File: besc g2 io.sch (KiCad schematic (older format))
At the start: 30 parts

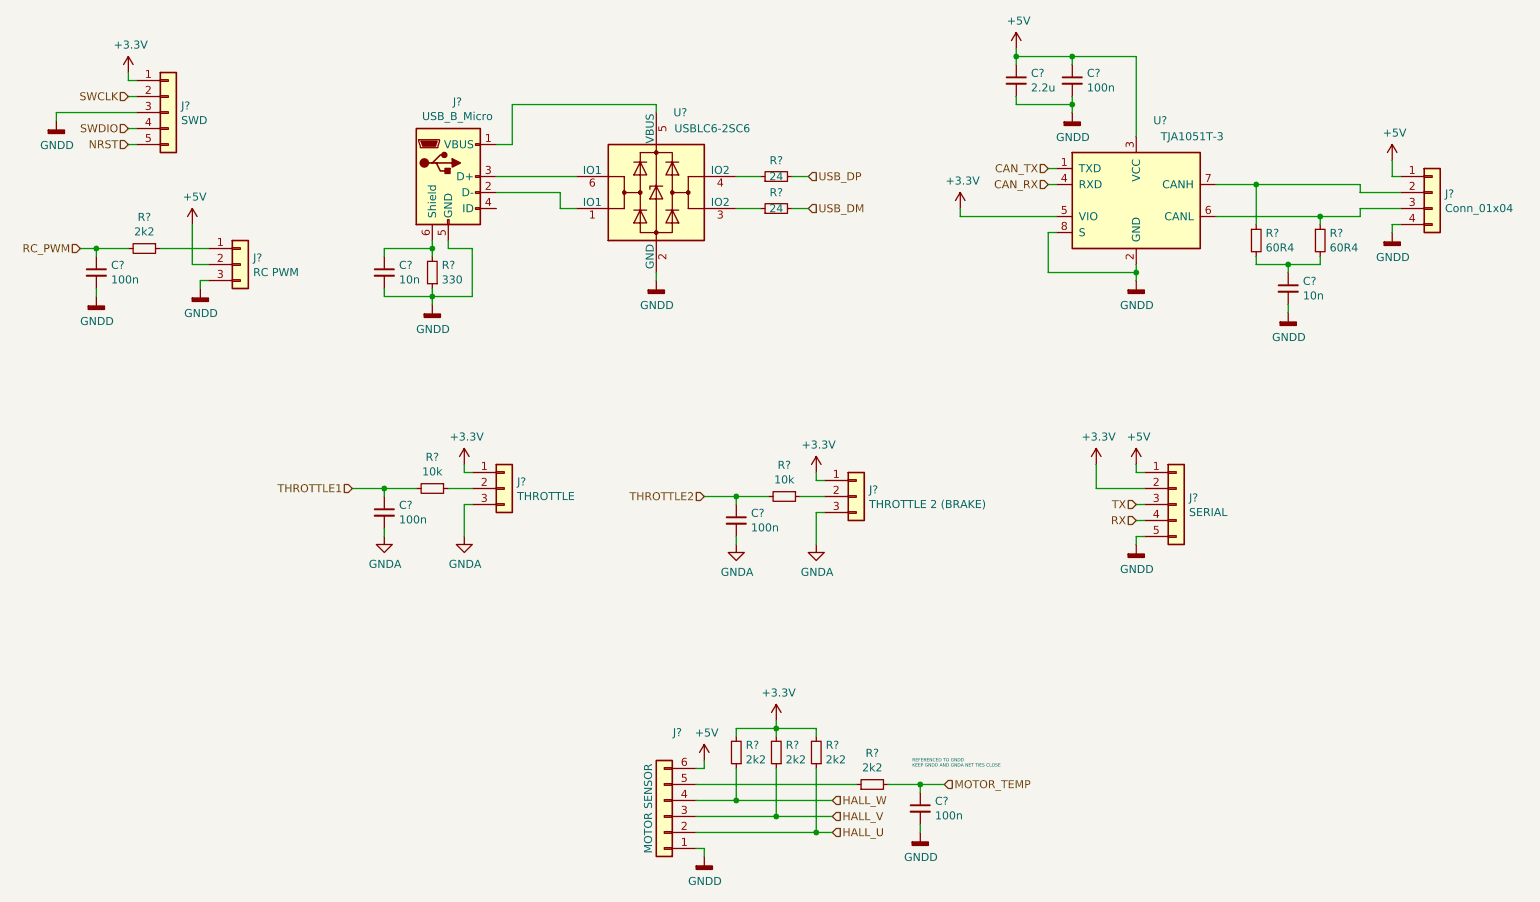
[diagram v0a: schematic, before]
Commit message: power stage layout draft
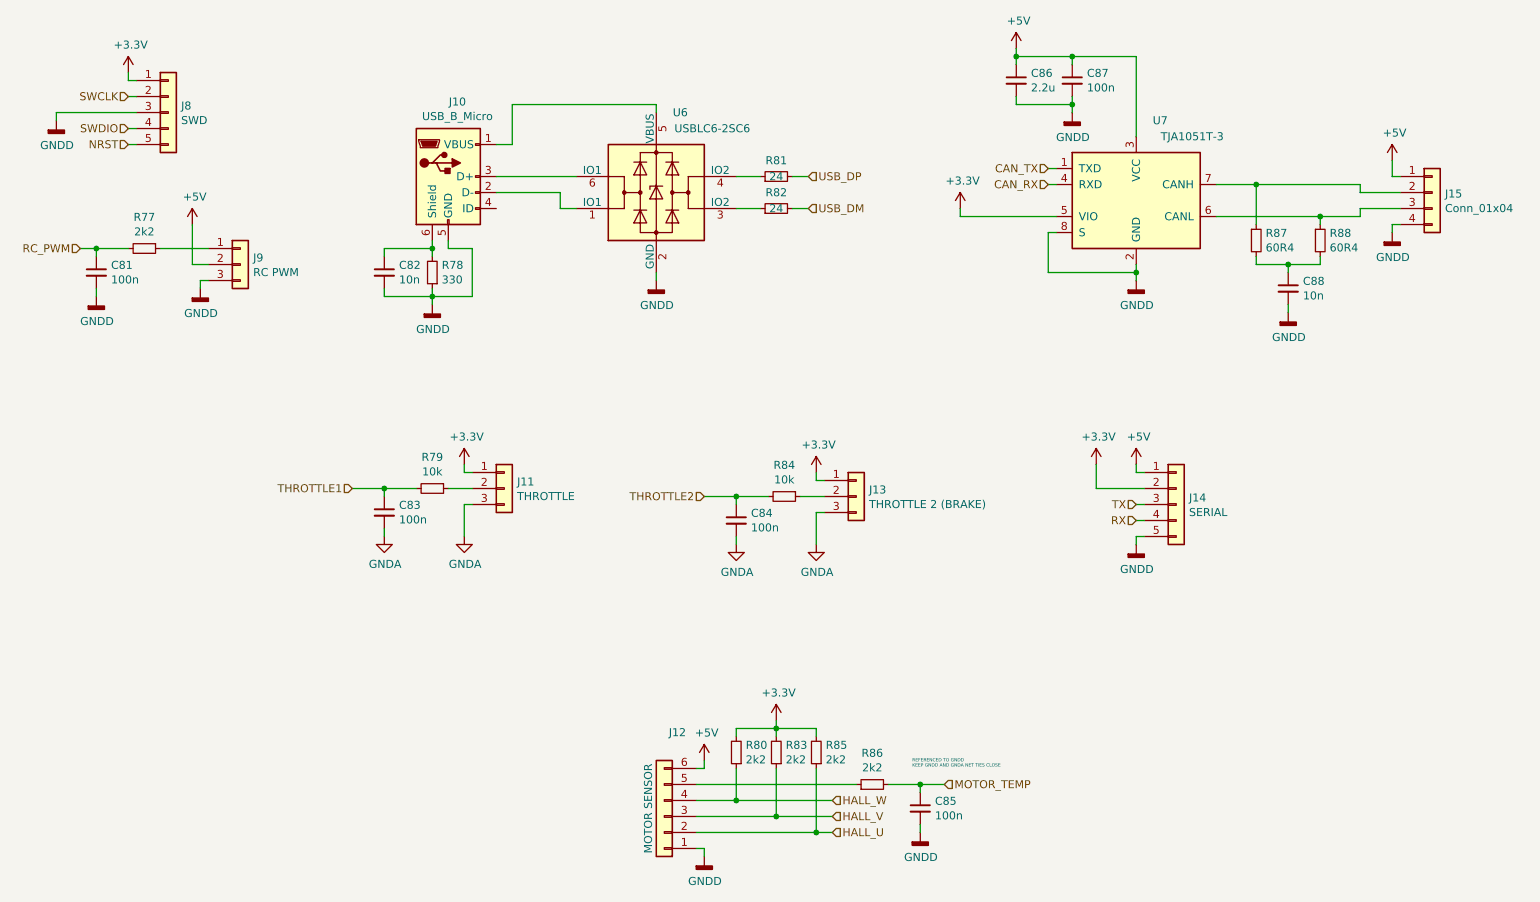
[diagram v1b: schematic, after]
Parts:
- C81, C82, C83, C84, C85, C86, C87, C88: renamed from C?; footprint (none) -> Capacitor_SMD:C_0603_1608Metric
- J10: renamed from J?; footprint (none) -> Connector_USB:USB_Micro-B_Molex_47346-0001
- J11: renamed from J?; footprint (none) -> Connector_PinHeader_2.54mm:PinHeader_1x03_P2.54mm_Vertical_SMD_Pin1Right
- J12: renamed from J?; footprint (none) -> Connector_PinHeader_2.54mm:PinHeader_1x06_P2.54mm_Vertical
- J13, J9: renamed from J?; footprint (none) -> Connector_PinHeader_2.54mm:PinHeader_1x03_P2.54mm_Vertical
- J14, J8: renamed from J?; footprint (none) -> Connector_PinHeader_2.54mm:PinHeader_1x05_P2.54mm_Vertical
- J15: renamed from J?; footprint (none) -> Connector_PinHeader_2.54mm:PinHeader_1x04_P2.54mm_Vertical
- R77, R78, R79, R80, R81, R82, R83, R84, R85, R86, R87, R88: renamed from R?; footprint (none) -> Resistor_SMD:R_0603_1608Metric
- gave numbers to parts that had none: 2

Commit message: isolated drivers, layout
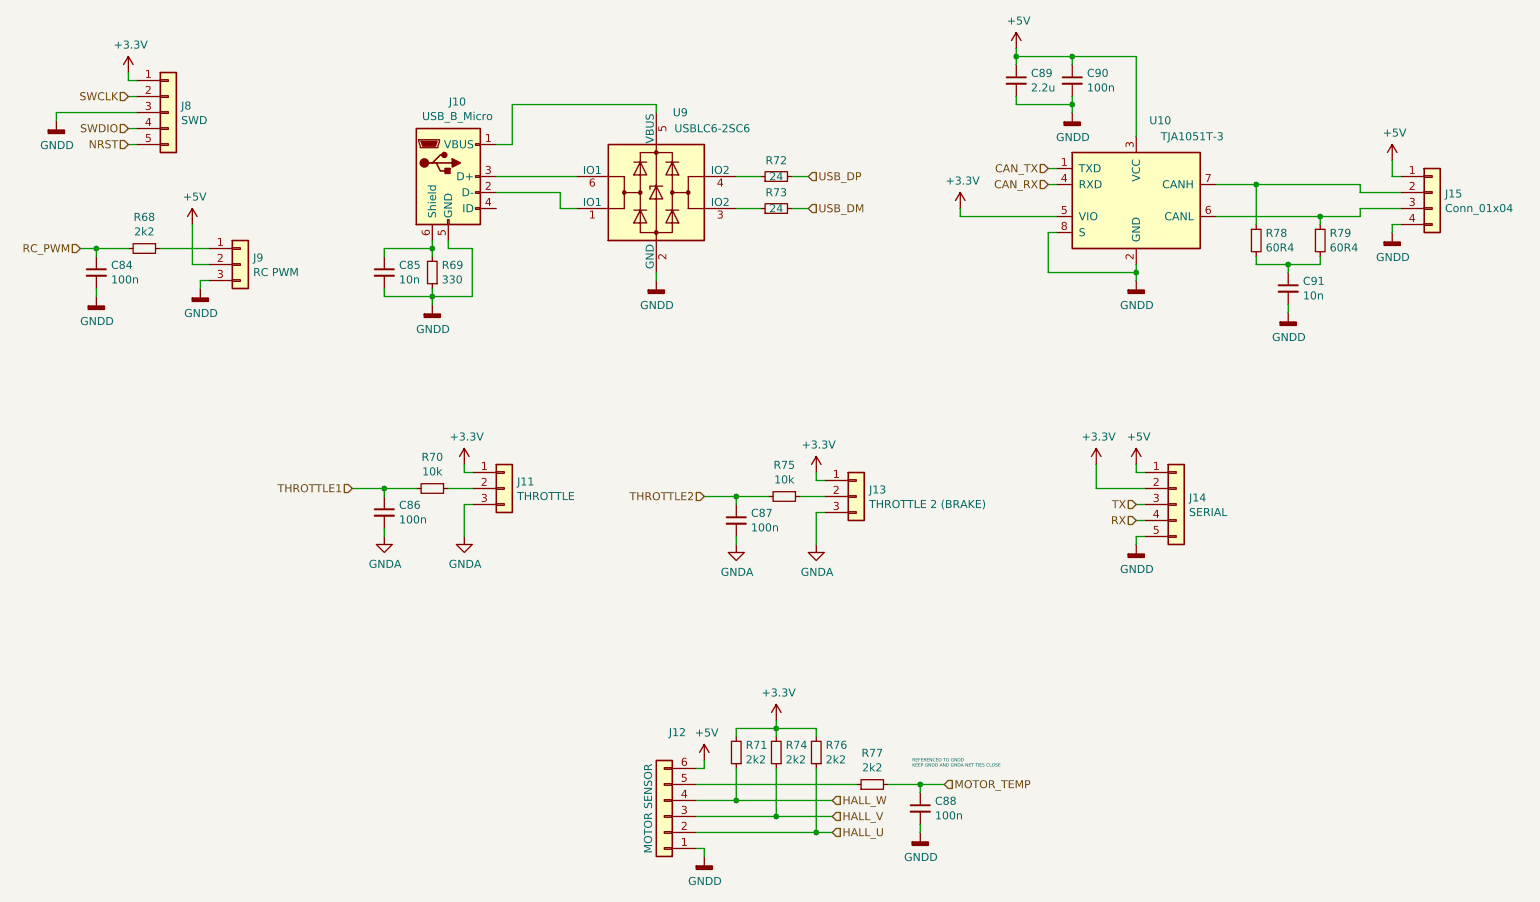
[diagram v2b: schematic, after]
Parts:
- renumbered C81 to C84, C82 to C85, C83 to C86, C84 to C87, C85 to C88, C86 to C89, C87 to C90, C88 to C91, R77 to R68, R78 to R69, R79 to R70, R80 to R71, R81 to R72, R82 to R73, R83 to R74, R84 to R75, R85 to R76, R86 to R77, R87 to R78, R88 to R79, U7 to U10, U6 to U9

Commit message: 12V PS, isolated gate drivers
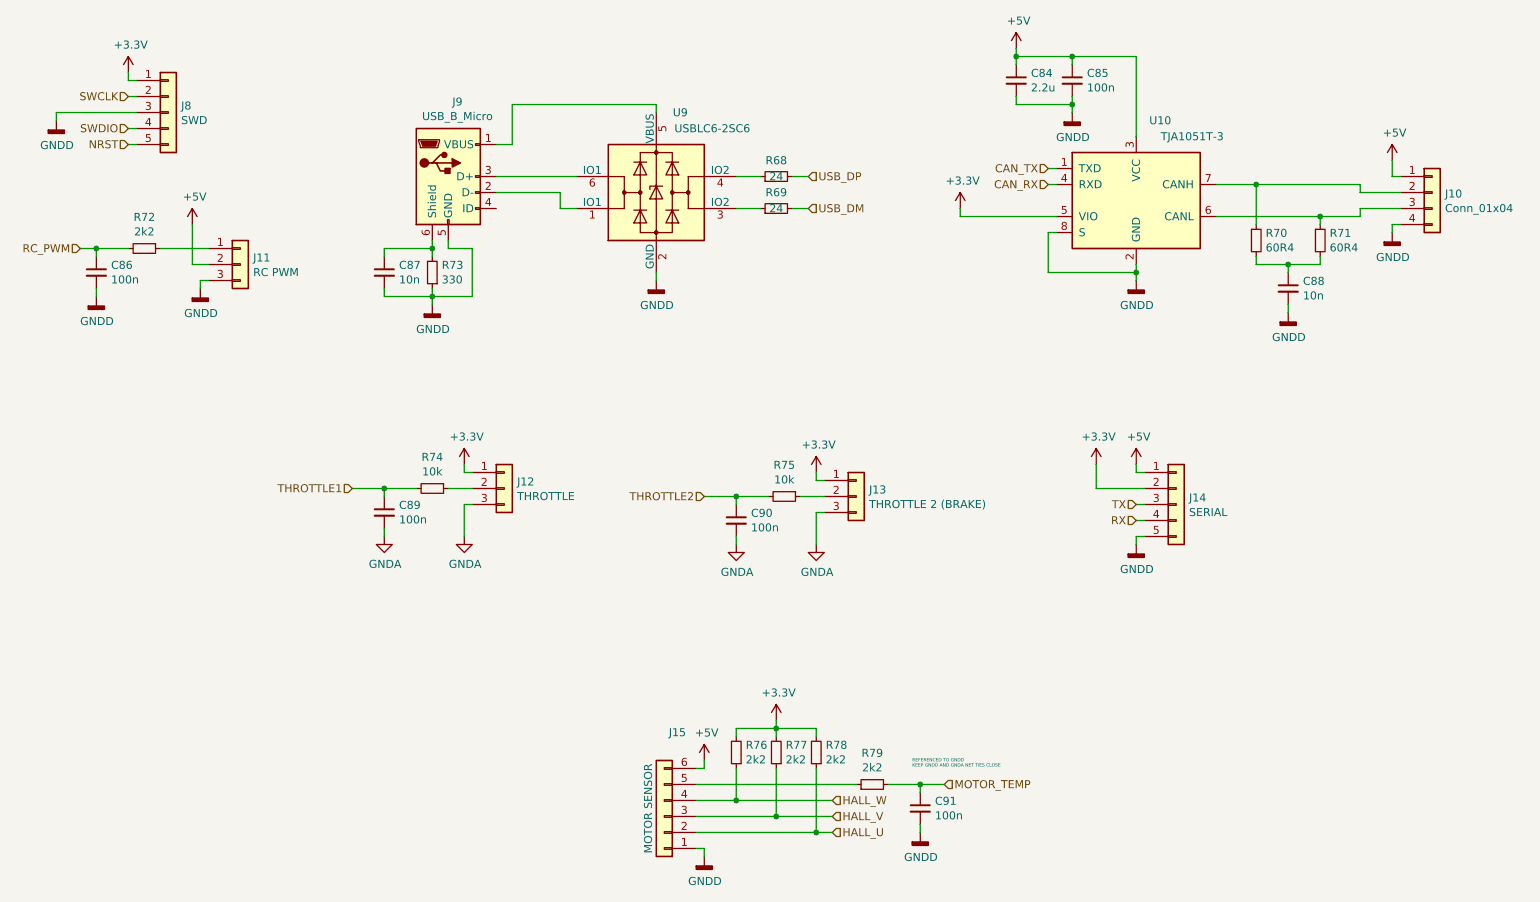
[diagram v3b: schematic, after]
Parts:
- renumbered C89 to C84, C90 to C85, C84 to C86, C85 to C87, C91 to C88, C86 to C89, C87 to C90, C88 to C91, J15 to J10, J9 to J11, J11 to J12, J12 to J15, J10 to J9, R72 to R68, R73 to R69, R78 to R70, R79 to R71, R68 to R72, R69 to R73, R70 to R74, R71 to R76, R74 to R77, R76 to R78, R77 to R79

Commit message: layout and routing progress
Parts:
- added D7: ESD 100V, Diode_SMD:D_SOD-123, symbol Device:D_Zener
- added J15: IGNITION, Connector_PinHeader_2.54mm:PinHeader_1x02_P2.54mm_Vertical, symbol Connector_Generic:Conn_01x02
- added R84, R85: 10k, Resistor_SMD:R_0603_1608Metric, symbol Device:R_Small
- J10: renamed from J9; footprint Connector_USB:USB_Micro-B_Molex_47346-0001 -> Connector_USB:USB_Micro-B_Wuerth_614105150721_Vertical_CircularHoles
- J11: renamed from J12; footprint Connector_PinHeader_2.54mm:PinHeader_1x03_P2.54mm_Vertical_SMD_Pin1Right -> Connector_PinHeader_2.54mm:PinHeader_1x03_P2.54mm_Vertical
- renumbered C86 to C84, C87 to C85, C89 to C86, C90 to C87, C91 to C88, C84 to C89, C85 to C90, C88 to C91, J15 to J12, J10 to J16, J11 to J9, R72 to R73, R73 to R74, R74 to R75, R68 to R77, R69 to R78, R77 to R79, R75 to R80, R78 to R81, R79 to R82, R70 to R83, R71 to R86
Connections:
- net GNDD: now also D7.2 (A)
- new net: J15.1 (Pin_1), R84.1
- new net: J15.2 (Pin_2), R85.1
- new net IGNITION: D7.1 (K), R85.2
- new net VDC: R84.2
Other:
- note added: "SHORT TO RUN"

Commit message: finished routing
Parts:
- J16: value Conn_01x04 -> CAN
- U9: footprint Package_TO_SOT_SMD:SOT-23-6 -> Package_TO_SOT_SMD:SOT-666
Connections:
- net at U9.1 (IO1): now also R77.1; no longer J10.2 (D-)
- net at U9.4 (IO2): now also J10.2 (D-); no longer R77.1
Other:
- moved on the sheet: R77
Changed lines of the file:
@@
 P 9800 1850
 F 0 "J16" H 9880 1842 50  0000 L CNN
-F 1 "Conn_01x04" H 9880 1751 50  0000 L CNN
+F 1 "CAN" H 9880 1751 50  0000 L CNN
 F 2 "Connector_PinHeader_2.54mm:PinHeader_1x04_P2.54mm_Vertical" H 9800 1850 50  0001 C CNN
 F 3 "~" H 9800 1850 50  0001 C CNN
@@
 F 0 "U9" H 5100 2350 50  0000 C CNN
 F 1 "USBLC6-2SC6" H 5300 2250 50  0000 C CNN
-F 2 "Package_TO_SOT_SMD:SOT-23-6" H 4200 2250 50  0001 C CNN
+F 2 "Package_TO_SOT_SMD:SOT-666" H 4200 2250 50  0001 C CNN
 F 3 "http://www2.st.com/resource/en/datasheet/CD00050750.pdf" H 5150 2200 50  0001 C CNN
 	1    4950 1850
@@
 Wire Wire Line
 	3950 1850 4350 1850
-Wire Wire Line
-	4350 1850 4350 1950
-Wire Wire Line
-	4350 1950 4450 1950
 Wire Wire Line
 	4450 1750 3950 1750
@@
 L Device:R_Small R77
 U 1 1 5DE3A02F
-P 5700 1750
-F 0 "R77" V 5800 1750 50  0000 C CNN
-F 1 "24" V 5700 1750 50  0000 C CNN
-F 2 "Resistor_SMD:R_0603_1608Metric" H 5700 1750 50  0001 C CNN
-F 3 "~" H 5700 1750 50  0001 C CNN
-	1    5700 1750
-	0    -1   -1   0
-$EndComp
-Wire Wire Line
-	5450 1750 5600 1750
+P 4250 2250
+F 0 "R77" V 4350 2250 50  0000 C CNN
+F 1 "24" V 4250 2250 50  0000 C CNN
+F 2 "Resistor_SMD:R_0603_1608Metric" H 4250 2250 50  0001 C CNN
+F 3 "~" H 4250 2250 50  0001 C CNN
+	1    4250 2250
+	1    0    0    -1
+$EndComp
 Wire Wire Line
 	5450 1950 5600 1950
-Text HLabel 5900 1750 2    50   Input ~ 0
+Text HLabel 4250 2450 3    50   Input ~ 0
 USB_DP
 Text HLabel 5900 1950 2    50   Input ~ 0
 USB_DM
 Wire Wire Line
-	5800 1750 5900 1750
+	4250 2350 4250 2450
 Wire Wire Line
 	5900 1950 5800 1950
@@
 Text Notes 9200 5700 0    50   ~ 0
 SHORT TO RUN
+Wire Wire Line
+	4450 1950 4250 1950
+Wire Wire Line
+	4250 1950 4250 2150
+Wire Wire Line
+	4350 1850 4350 1150
+Wire Wire Line
+	4350 1150 5700 1150
+Wire Wire Line
+	5700 1150 5700 1750
+Wire Wire Line
+	5700 1750 5450 1750
 $EndSCHEMATC
